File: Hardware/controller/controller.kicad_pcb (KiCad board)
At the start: 4 copper layers, 128.1 x 184.5 mm, 70 parts, among them J101 Conn_02x10_Odd_Even, J102 Conn_02x10_Odd_Even, J301 Conn_ARM_JTAG_SWD_10, SW301 B3F-1005, U201 BD9C301FJ, U301 AT24CS32-SSHM, U302 ATSAME51J20A-A, Y301 32.768kHz, Y302 12MHz

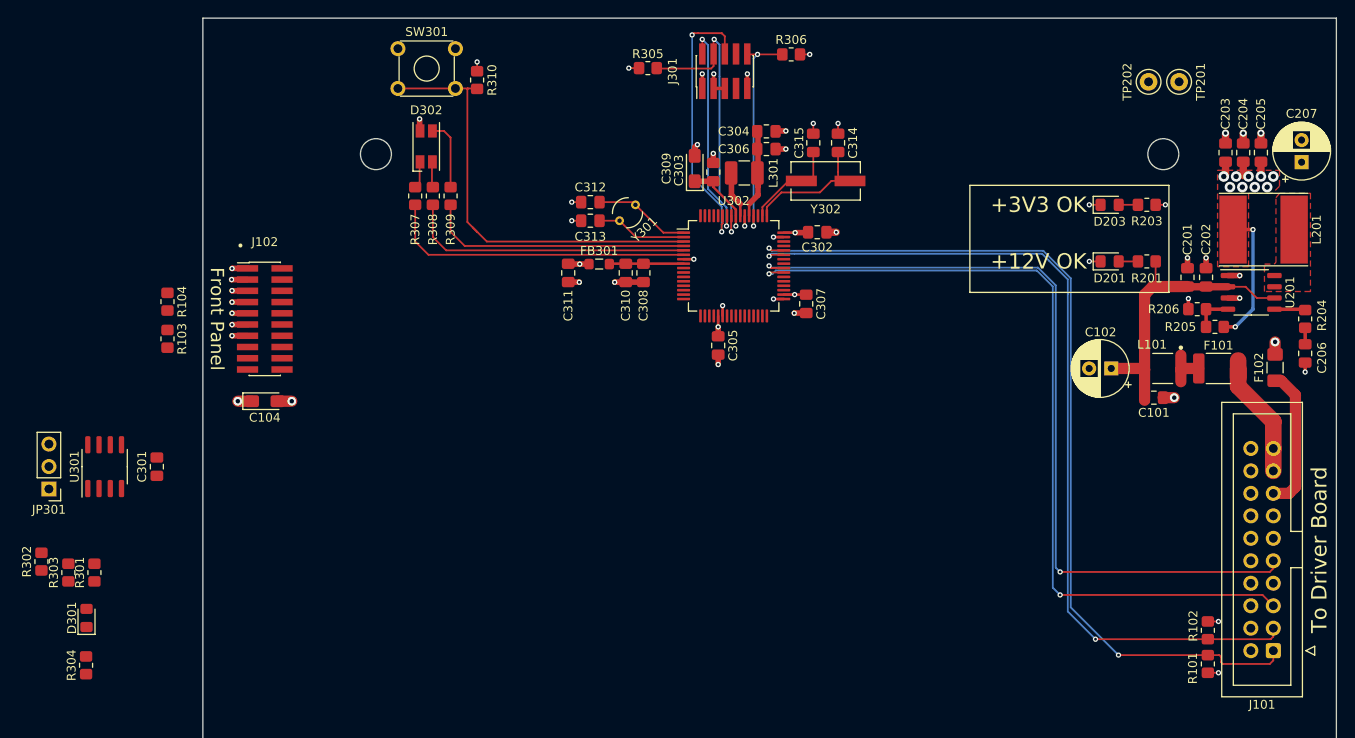
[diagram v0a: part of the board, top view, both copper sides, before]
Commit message: Basic controller board finished
- This just has the connections to the front panel and driver board; it
  lacks the rear IO connectors, a power button, and the Ethernet PHY
  currently
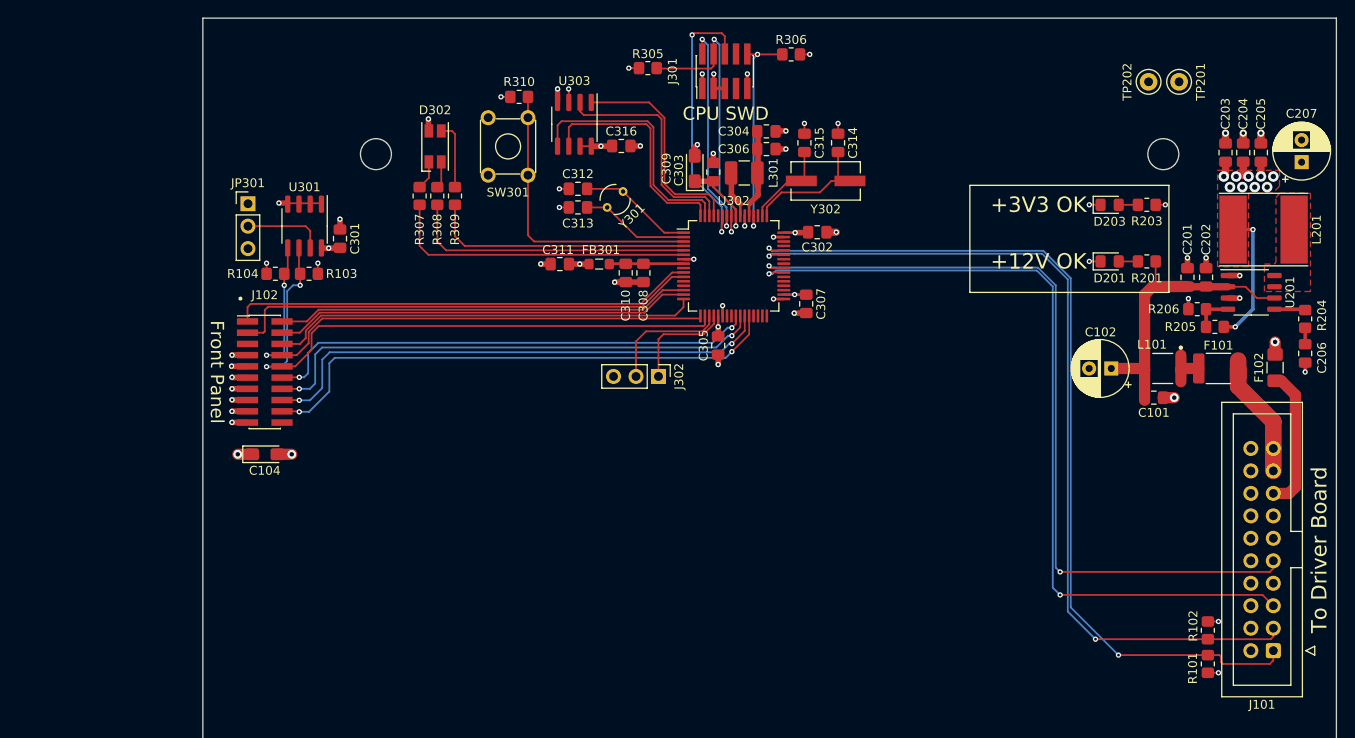
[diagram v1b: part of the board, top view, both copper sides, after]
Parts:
- removed D301: Red, LED_SMD:LED_0805_2012Metric_Pad1.15x1.40mm_HandSolder
- removed R301, R303: 1k, Resistor_SMD:R_0805_2012Metric_Pad1.20x1.40mm_HandSolder
- removed R302: 2k2, Resistor_SMD:R_0805_2012Metric_Pad1.20x1.40mm_HandSolder
- removed R304: 10k, Resistor_SMD:R_0805_2012Metric_Pad1.20x1.40mm_HandSolder
- added C316: 100nF, Capacitor_SMD:C_0805_2012Metric_Pad1.18x1.45mm_HandSolder, F.Cu at (67.3, 34.5)
- added J302: Conn_01x03_Male, Connector_PinHeader_2.54mm:PinHeader_1x03_P2.54mm_Vertical, F.Cu at (71.5, 60.5)
- added U303: AT25SF321B-SSHB, Package_SO:SOIC-8_3.9x4.9mm_P1.27mm, F.Cu at (62.0, 32.0)
- moved JP301 39.3 mm to (25.1, 41.0), turned to 0 degrees
- moved U301 35.4 mm to (31.5, 43.5), turned to -90 degrees
- moved C301 33.1 mm to (35.5, 44.9)
- moved R103 17.6 mm to (32.0, 48.9), turned to 0 degrees
- moved R104 12.6 mm to (28.2, 48.9), turned to 180 degrees
- moved SW301 8.84 mm to (56.8, 31.2), turned to -90 degrees
- moved C104 6.00 mm to (27.0, 69.3)
- moved J102 6.00 mm to (27.0, 60.0)
- moved R310 5.12 mm to (55.8, 28.9), turned to 180 degrees
- moved C312 2.05 mm to (62.4, 39.3)
- moved C313 2.05 mm to (62.4, 41.4)
- moved Y301 2.05 mm to (67.5, 39.6)
- moved C311 1.38 mm to (60.4, 47.8), turned to 180 degrees
- moved C315 1.00 mm to (88.0, 34.1)
- moved D302 1.00 mm to (46.2, 34.5)
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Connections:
- J102 pad 1: GND -> /FRONT_ENC_A
- J102 pad 10: /DISP_D/~{C} -> /FRONT_SCL
- J102 pad 11: +3V3 -> GND
- J102 pad 12: /~{DISP_RESET} -> /DISP_MISO
- J102 pad 13: +3V3 -> GND
- J102 pad 14: unconnected-(J102-Pad14) -> /DISP_SCK
- J102 pad 15: unconnected-(J102-Pad15) -> GND
- J102 pad 16: /~{FRONT_IRQ} -> /~{DISP_CS}
- J102 pad 17: /FRONT_ENC_B -> +3V3
- J102 pad 18: /FRONT_SDA -> /DISP_MOSI
- J102 pad 19: /FRONT_ENC_A -> +3V3
- J102 pad 2: /DISP_MISO -> /DISP_D/~{C}
- J102 pad 20: /FRONT_SCL -> unconnected-(J102-Pad20)
- J102 pad 3: GND -> /FRONT_ENC_B
- J102 pad 4: /DISP_MOSI -> /~{DISP_RESET}
- J102 pad 5: GND -> unconnected-(J102-Pad5)
- J102 pad 6: /DISP_SCK -> /~{FRONT_IRQ}
- J102 pad 8: /~{DISP_CS} -> /FRONT_SDA
- U302 pad 62: /CPU/NOR_MOSI -> /CPU/NOR_MISO
- U302 pad 63: /CPU/NOR_MISO -> /CPU/NOR_MOSI
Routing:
- net /FRONT_SCL: track 0.00 -> 70.1 mm, vias 0 -> 2
- net /FRONT_SDA: track 0.00 -> 65.5 mm, vias 0 -> 2
- net /DISP_MOSI: track 0.00 -> 60.4 mm, vias 0 -> 2
- net /~{DISP_CS}: track 0.00 -> 59.1 mm, vias 0 -> 2
- net /DISP_SCK: track 0.00 -> 57.9 mm, vias 0 -> 2
- net /DISP_MISO: track 0.00 -> 56.1 mm, vias 0 -> 2
- net /FRONT_ENC_B: track 0.00 -> 53.3 mm
- net /FRONT_ENC_A: track 0.00 -> 52.5 mm
- net /~{FRONT_IRQ}: track 0.00 -> 48.5 mm
- net /~{DISP_RESET}: track 0.00 -> 47.2 mm
- net /DISP_D/~{C}: track 0.00 -> 46.9 mm
- net /CPU/NOR_MOSI: track 0.00 -> 28.3 mm
- net /CPU/NOR_SCK: track 0.00 -> 26.0 mm
- net /CPU/NOR_MISO: track 0.00 -> 25.8 mm
- net /CPU/~{NOR_CS}: track 0.00 -> 24.6 mm
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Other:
- board text added: "CPU SWD"
- board text added: "Cfg WP"
- board text added: "GND"
- board text added: "Off"
- board text added: "On"
- board text added: "RXD"
- board text added: "TXD"

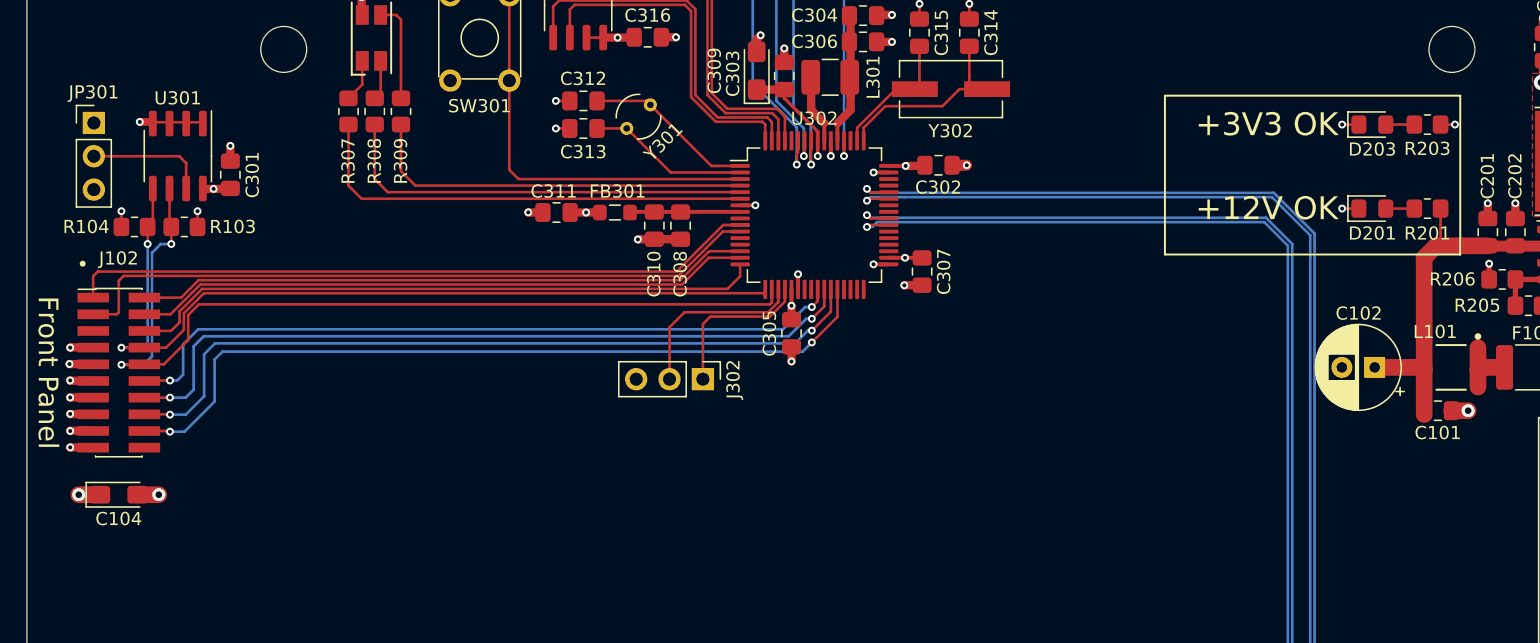
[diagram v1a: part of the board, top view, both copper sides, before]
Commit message: Added basic rear IO connector
- Placed the connector for the rear IO board, which will carry USB, I2C,
  Ethernet and power. Currently, USB and I2C have been hooked up.

- Added an I2C switch. This will allow sharing the secondary I2C bus
  between the front panel and rear IO, without needing to worry about
  address conflicts or other such issues.

  Removed the on-board I2C EEPROM; we have a NOR flash instead.
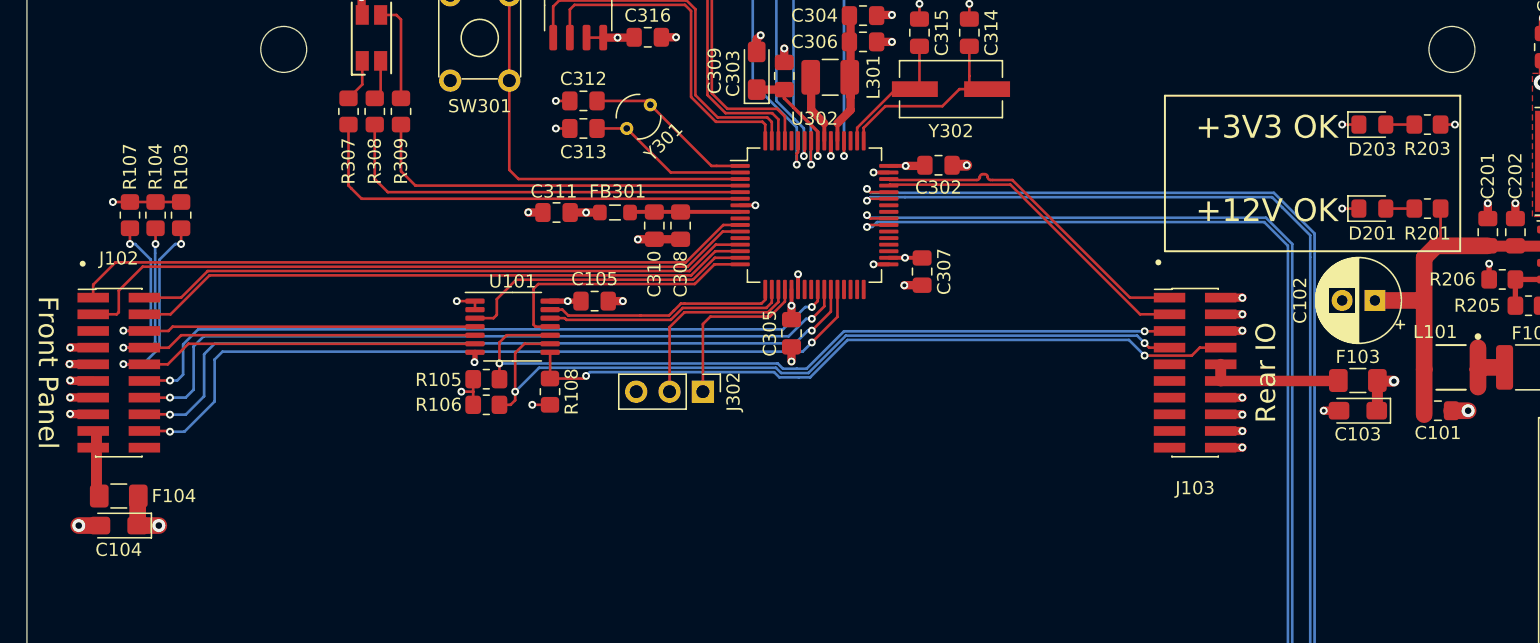
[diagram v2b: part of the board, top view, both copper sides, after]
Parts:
- removed C301: 100nF, Capacitor_SMD:C_0805_2012Metric_Pad1.18x1.45mm_HandSolder
- removed JP301: Cfg WP, Connector_PinHeader_2.54mm:PinHeader_1x03_P2.54mm_Vertical
- removed U301: AT24CS32-SSHM, Package_SO:SOIC-8_3.9x4.9mm_P1.27mm
- added C103: 10µF, Capacitor_Tantalum_SMD:CP_EIA-3216-18_Kemet-A_Pad1.58x1.35mm_HandSolder, F.Cu at (121.4, 62.9)
- added C105: 100nF, Capacitor_SMD:C_0805_2012Metric_Pad1.18x1.45mm_HandSolder, F.Cu at (63.2, 54.5)
- added F103: 250mA, Fuse:Fuse_1206_3216Metric_Pad1.42x1.75mm_HandSolder, F.Cu at (121.4, 60.6)
- added F104: 500mA, Fuse:Fuse_1206_3216Metric_Pad1.42x1.75mm_HandSolder, F.Cu at (27.0, 69.4)
- added J103: Conn_02x10_Odd_Even, Connector_PinHeader_1.27mm:PinHeader_2x10_P1.27mm_Vertical_SMD, F.Cu at (109.0, 60.0)
- added R105: 2k2, Resistor_SMD:R_0805_2012Metric_Pad1.20x1.40mm_HandSolder, F.Cu at (55.0, 60.5)
- added R106: 2k2, Resistor_SMD:R_0805_2012Metric_Pad1.20x1.40mm_HandSolder, F.Cu at (55.0, 62.5)
- added R107: 10k, Resistor_SMD:R_0805_2012Metric_Pad1.20x1.40mm_HandSolder, F.Cu at (27.9, 48.0)
- added R108: 10k, Resistor_SMD:R_0805_2012Metric_Pad1.20x1.40mm_HandSolder, F.Cu at (59.9, 61.5)
- added U101: PCA9543A, Package_SO:TSSOP-14_4.4x5mm_P0.65mm, F.Cu at (57.0, 56.5)
- F101: value 500mA -> 1A
- moved C102 5.10 mm to (122.7, 54.5)
- moved C104 2.35 mm to (27.0, 71.7), turned to 180 degrees
- moved R104 1.84 mm to (29.8, 48.0), turned to 90 degrees
- moved J302 0.95 mm to (71.5, 61.5)
- moved R103 0.93 mm to (31.8, 48.0), turned to 90 degrees
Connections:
- J102 pad 17: +3V3 -> Net-(J102-Pad17)
- J102 pad 19: +3V3 -> Net-(J102-Pad17)
- U302 pad 13: unconnected-(U302-Pad13) -> /DISP_D/~{C}
- U302 pad 14: /DISP_D/~{C} -> /~{DISP_RESET}
- U302 pad 15: /~{DISP_RESET} -> /~{I2C_RESET}
- U302 pad 16: /~{FRONT_IRQ} -> /~{I2C_IRQ}
- U302 pad 17: /FRONT_SDA -> /I2C_SDA
- U302 pad 18: /FRONT_SCL -> /I2C_SCL
- U302 pad 45: /CPU/USB_D- -> /USB_D-
- U302 pad 46: /CPU/USB_D+ -> /USB_D+
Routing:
- net /IO_SDA: track 0.00 -> 60.2 mm, vias 0 -> 2
- net /IO_SCL: track 0.00 -> 59.3 mm, vias 0 -> 2
- net /~{IO_IRQ}: track 0.00 -> 55.4 mm, vias 0 -> 2
- net /FRONT_SCL: track 70.1 -> 40.8 mm
- net /FRONT_SDA: track 65.5 -> 38.5 mm
- net /USB_D+: track 0.00 -> 25.6 mm
- net /USB_D-: track 0.00 -> 25.5 mm
- net /~{I2C_RESET}: track 0.00 -> 22.8 mm
- net /~{I2C_IRQ}: track 0.00 -> 20.6 mm
- net /I2C_SCL: track 0.00 -> 18.5 mm
- net /I2C_SDA: track 0.00 -> 17.9 mm
- net /~{FRONT_IRQ}: track 48.5 -> 37.5 mm, vias 0 -> 2
- net GND: track 61.4 -> 72.1 mm, vias 42 -> 51
- net Net-(J103-Pad10): track 0.00 -> 10.2 mm
- net +3V3: track 64.6 -> 74.2 mm
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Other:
- board text added: "Rear IO"
- board text removed: "Cfg WP"
- board text removed: "Off"
- board text removed: "On"
